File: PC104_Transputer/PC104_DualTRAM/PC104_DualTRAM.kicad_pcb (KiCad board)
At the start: 4 copper layers, 95.9 x 90.2 mm, 41 parts, among them J1 Conn_02x32_Odd_Even, J10 Conn_02x30_Row_Letter_First, J2 Conn_02x20_Odd_Even, J3 UPSTREAM, J4 DOWNSTREAM, J5 Conn_01x02, J6 Conn_01x02, J9 Conn_02x30_Row_Letter_First, U1 TRAM, U2 74LS244_Split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

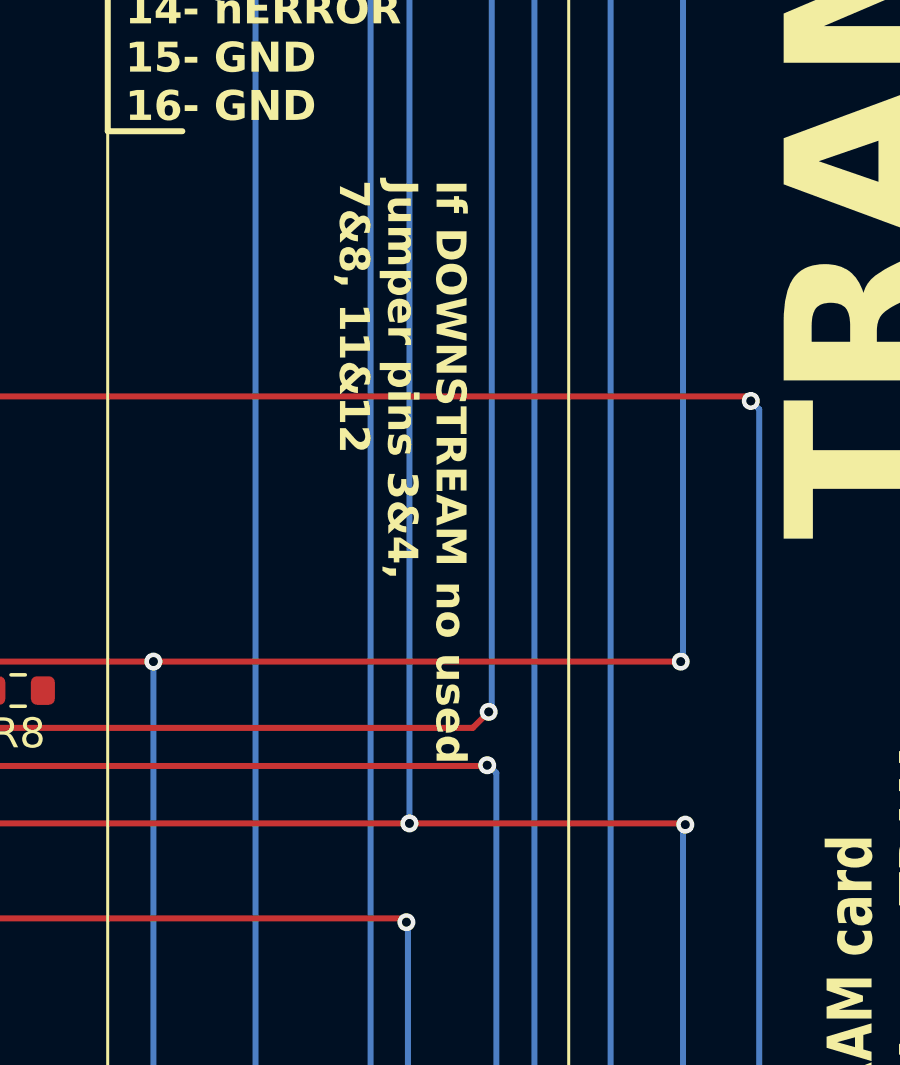
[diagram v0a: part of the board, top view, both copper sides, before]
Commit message: Fixed CPLD pinout
Fixed the CPLD pin out which would never have worked with the previous version due to the PLCC and TQFP pinouts being different
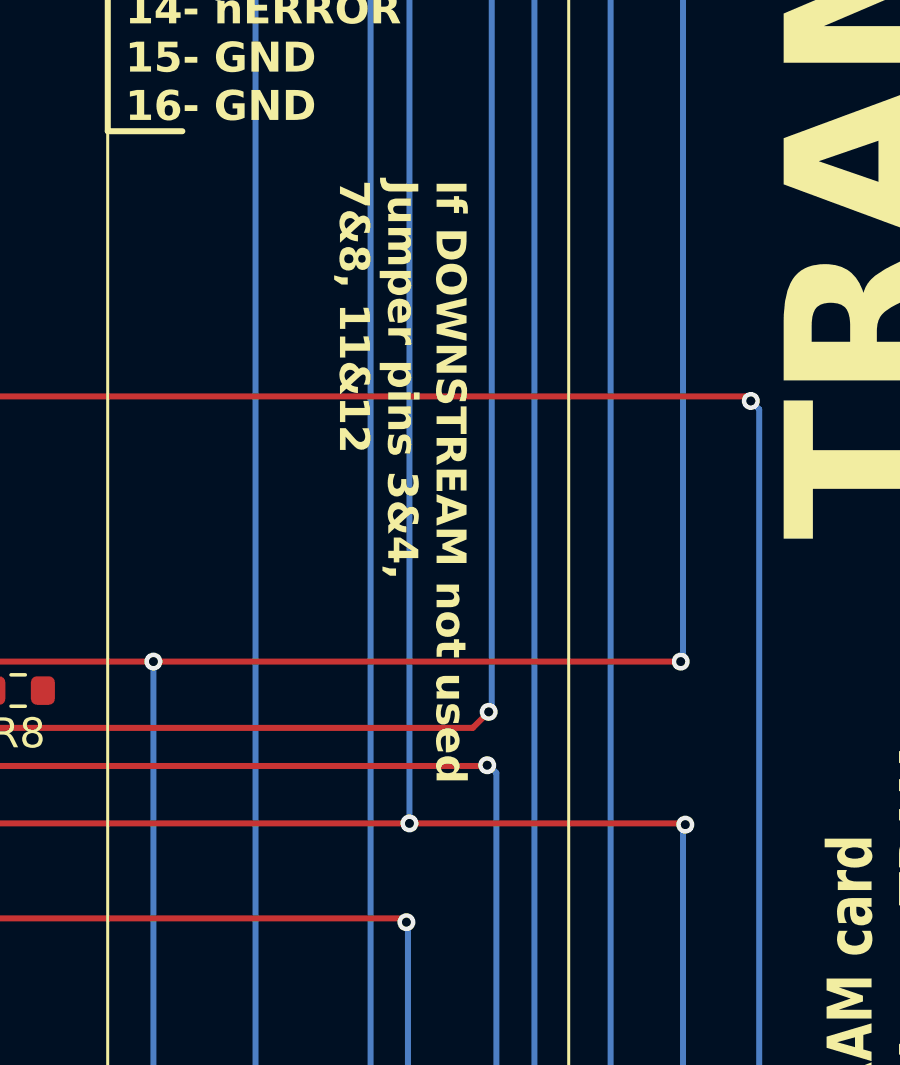
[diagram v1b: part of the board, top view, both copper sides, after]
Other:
- board text added: "If DOWNSTREAM not used Jumper pins 3&4, 7&8, 11&12"
- board text removed: "If DOWNSTREAM no used Jumper pins 3&4, 7&8, 11&12"
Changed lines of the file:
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@@
 		)
 	)
-	(gr_text "If DOWNSTREAM no used\nJumper pins 3&4, \n7&8, 11&12"
+	(gr_text "If DOWNSTREAM not used\nJumper pins 3&4, \n7&8, 11&12"
 		(at 146.304 90.4748 270)
 		(layer "F.SilkS")
@@
 		(net_name "")
 		(locked yes)
-		(layers "F.Cu" "Dwgs.User")
+		(layers "F.Cu" "In1.Cu" "Dwgs.User")
 		(hatch edge 0.5)
 		(connect_pads
@@
 		(net_name "")
 		(locked yes)
-		(layers "F.Cu" "Dwgs.User")
+		(layers "F.Cu" "In1.Cu" "Dwgs.User")
 		(hatch edge 0.5)
 		(connect_pads
@@
 		(net_name "")
 		(locked yes)
-		(layer "B.Cu")
+		(layers "B.Cu" "In2.Cu")
 		(hatch edge 0.5)
 		(connect_pads
@@
 		(net_name "")
 		(locked yes)
-		(layer "B.Cu")
+		(layers "B.Cu" "In2.Cu")
 		(hatch edge 0.5)
 		(connect_pads
